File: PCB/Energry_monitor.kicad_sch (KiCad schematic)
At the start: 0 parts

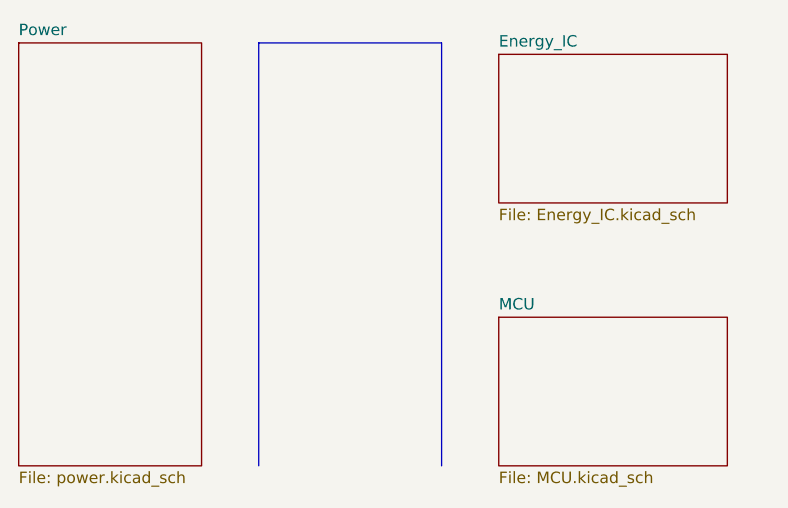
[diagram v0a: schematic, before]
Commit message: added firmware dir
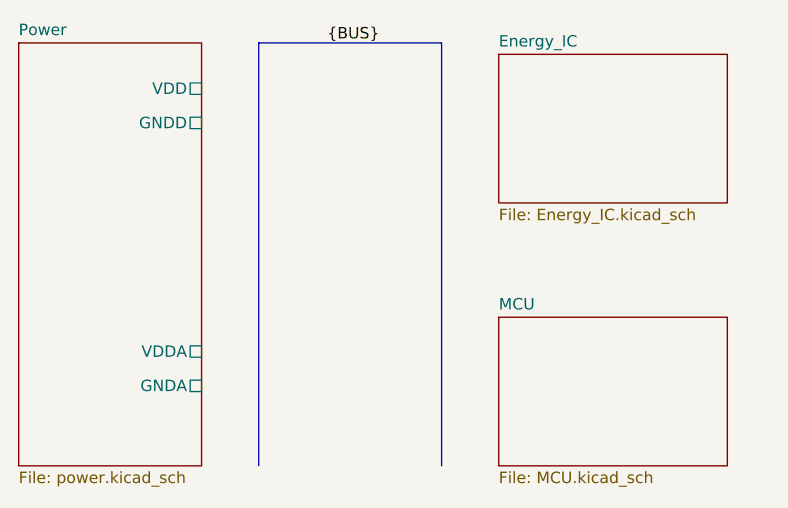
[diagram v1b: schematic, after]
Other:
- sheet Power ports: added GNDA, GNDD, VDD, VDDA; removed none
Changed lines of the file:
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@@
 	(generator_version "9.0")
 	(paper "A4")
+	(bus_alias "BUS"
+		(members "VDD")
+	)
 	(bus
 		(pts
@@
 			(width 0)
 			(type default)
+		)
+	)
+	(label "{BUS}"
+		(at 142.24 68.58 0)
+		(effects
+			(font
+				(size 1.27 1.27)
+			)
+			(justify left bottom)
 		)
 	)
@@
 			)
 		)
+		(pin "VDD" passive
+			(at 128.27 73.66 0)
+			(effects
+				(font
+					(size 1.27 1.27)
+				)
+				(justify right)
+			)
+		)
+		(pin "GNDD" passive
+			(at 128.27 77.47 0)
+			(effects
+				(font
+					(size 1.27 1.27)
+				)
+				(justify right)
+			)
+		)
+		(pin "VDDA" passive
+			(at 128.27 102.87 0)
+			(effects
+				(font
+					(size 1.27 1.27)
+				)
+				(justify right)
+			)
+		)
+		(pin "GNDA" passive
+			(at 128.27 106.68 0)
+			(effects
+				(font
+					(size 1.27 1.27)
+				)
+				(justify right)
+			)
+		)
